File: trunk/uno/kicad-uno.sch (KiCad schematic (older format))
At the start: 17 parts, among them J1 RESET_EN, SW1 RESET

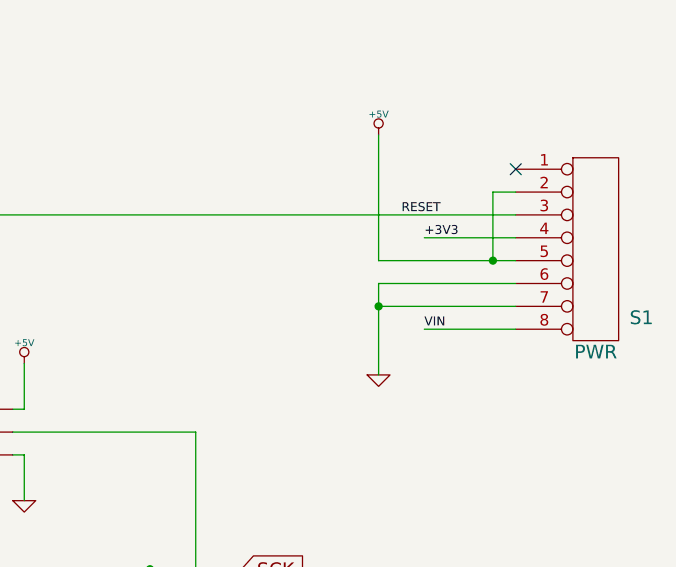
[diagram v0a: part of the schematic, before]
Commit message: Schematic ERC passes. Circuit _might_ be complete, without errors. You just never know. :-P
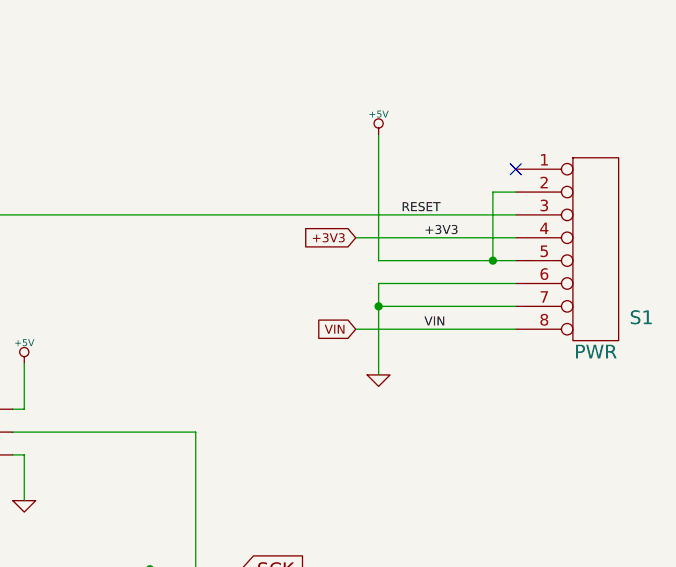
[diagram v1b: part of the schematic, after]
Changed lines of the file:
@@
 Connection ~ 3750 2150
-Wire Wire Line
-	8350 1450 7950 1450
 Wire Wire Line
 	8350 1650 7750 1650
@@
 	8350 1750 7750 1750
 Connection ~ 7750 1750
-Wire Wire Line
-	8350 1850 7950 1850
 Connection ~ 6950 3900
 Connection ~ 6850 3800
@@
 	7950 3600 7950 4350
 Connection ~ 6750 2900
+Text GLabel 7650 1450 0    39   Input ~ 0
++3V3
+Wire Wire Line
+	8350 1450 7650 1450
+Text GLabel 7650 1850 0    39   Input ~ 0
+VIN
+Wire Wire Line
+	8350 1850 7650 1850
 $EndSCHEMATC

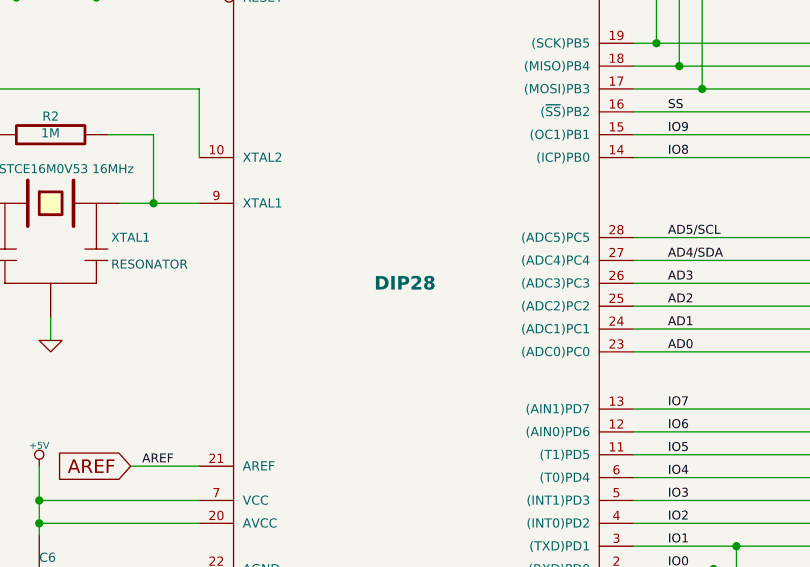
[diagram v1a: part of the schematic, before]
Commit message: Component packages configured.
PCB initial placement.

Some minor typo corrections.
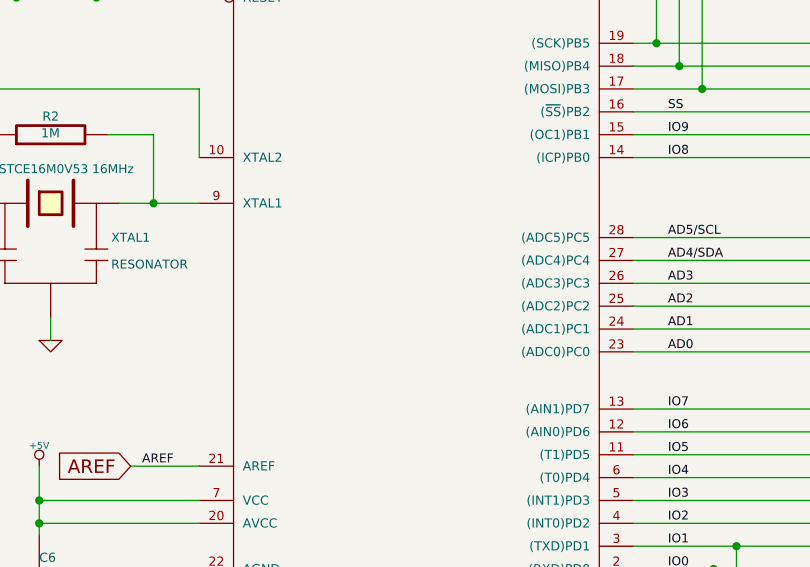
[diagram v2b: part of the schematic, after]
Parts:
- C5, C6: footprint ~ -> SM0603_Capa
- D2: footprint ~ -> SM1206D
- ICSP1: footprint (none) -> pin_array_3x2
- J1: footprint ~ -> JSOLD
- R2, RN1D1, RN2D1, RN4A1, RN4B1, SW1, XTAL1: footprint ~ -> (none)
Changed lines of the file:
@@
 Sheet 1 3
 Title "KiCADuino UNO Rev3"
-Date "24 jul 2013"
+Date "25 jul 2013"
 Rev "0.1"
 Comp "Gruvin & Co"
@@
 F 0 "R2" V 4180 4100 40  0000 C CNN
 F 1 "1M" V 4107 4101 40  0000 C CNN
-F 2 "~" V 4030 4100 30  0000 C CNN
+F 2 "" V 4030 4100 30  0001 C CNN
 F 3 "~" H 4100 4100 30  0000 C CNN
 	1    4100 4100
@@
 F 0 "XTAL1" H 4450 4250 39  0000 C CNN
 F 1 "CSTCE16M0V53 16MHz" H 4150 4550 39  0000 C CNN
-F 2 "~" H 4100 4400 60  0000 C CNN
+F 2 "" H 4100 4400 60  0001 C CNN
 F 3 "~" H 4100 4400 60  0000 C CNN
 	1    4100 4400
@@
 F 0 "ZU4" H 4950 6300 47  0000 L BNN
 F 1 "ATMEGA328P-PU" H 5850 3200 47  0000 L BNN
-F 2 "DIP28" H 5650 4850 59  0000 C CNB
+F 2 "DIP28" H 5650 4850 59  0001 C CNB
 F 3 "~" H 5650 4800 60  0000 C CNN
 	1    5650 4800
@@
 F 0 "C6" H 4050 6150 40  0000 L CNN
 F 1 "100n" H 4056 5965 40  0000 L CNN
-F 2 "~" H 4088 5900 30  0000 C CNN
+F 2 "SM0603_Capa" H 4088 5900 30  0001 C CNN
 F 3 "~" H 4050 6050 60  0000 C CNN
 	1    4050 6050
@@
 F 0 "D2" H 4300 3300 40  0000 C CNN
 F 1 "CD1206-S01575" H 4300 3100 40  0000 C CNN
-F 2 "~" H 4300 3200 60  0000 C CNN
+F 2 "SM1206D" H 4300 3200 60  0001 C CNN
 F 3 "~" H 4300 3200 60  0000 C CNN
 	1    4300 3200
@@
 F 0 "RN1D1" V 4030 3200 40  0000 C CNN
 F 1 "10K" V 3957 3201 40  0000 C CNN
-F 2 "~" V 3880 3200 30  0000 C CNN
+F 2 "" V 3880 3200 30  0001 C CNN
 F 3 "~" H 3950 3200 30  0000 C CNN
 	1    3950 3200
@@
 F 0 "ICSP1" H 5750 2600 50  0000 C CNN
 F 1 "3X2 M" H 5750 2200 40  0000 C CNN
-F 2 "" H 5750 2350 60  0000 C CNN
+F 2 "pin_array_3x2" H 5750 2350 60  0001 C CNN
 F 3 "" H 5750 2350 60  0000 C CNN
 	1    5750 2350
@@
 F 0 "SW1" V 4200 2300 60  0000 L CNN
 F 1 "RESET" V 4350 2300 60  0000 L CNN
-F 2 "~" H 4300 1950 60  0000 C CNN
+F 2 "" H 4300 1950 60  0001 C CNN
 F 3 "~" H 4300 1950 60  0000 C CNN
 	1    4300 1950
@@
 F 0 "J1" H 3350 2300 60  0000 C CNN
 F 1 "RESET_EN" H 3350 2070 40  0000 C CNN
-F 2 "~" H 3350 2150 60  0000 C CNN
+F 2 "JSOLD" H 3350 2150 60  0001 C CNN
 F 3 "~" H 3350 2150 60  0000 C CNN
 	1    3350 2150
@@
 F 0 "C5" V 2750 2250 40  0000 L CNN
 F 1 "100n" V 2650 2200 40  0000 L CNN
-F 2 "~" H 2738 2250 30  0000 C CNN
+F 2 "SM0603_Capa" H 2738 2250 30  0001 C CNN
 F 3 "~" H 2700 2400 60  0000 C CNN
 	1    2700 2400
@@
 F 0 "S4" H 8900 4150 60  0000 C CNN
 F 1 "IOH" H 8700 4300 60  0000 C CNN
-F 2 "" H 8700 3750 60  0000 C CNN
+F 2 "" H 8700 3750 60  0001 C CNN
 F 3 "" H 8700 3750 60  0000 C CNN
 	1    8700 3750
@@
 F 0 "S2" H 8900 5000 60  0000 C CNN
 F 1 "AD" H 8700 5150 60  0000 C CNN
-F 2 "" H 8700 4800 60  0000 C CNN
+F 2 "" H 8700 4800 60  0001 C CNN
 F 3 "" H 8700 4800 60  0000 C CNN
 	1    8700 4800
@@
 F 0 "S3" H 8900 5950 60  0000 C CNN
 F 1 "IOL" H 8700 6150 60  0000 C CNN
-F 2 "" H 8700 5650 60  0000 C CNN
+F 2 "" H 8700 5650 60  0001 C CNN
 F 3 "" H 8700 5650 60  0000 C CNN
 	1    8700 5650
@@
 F 0 "S1" H 8900 1200 60  0000 C CNN
 F 1 "PWR" H 8700 1050 60  0000 C CNN
-F 2 "" H 8700 1500 60  0000 C CNN
+F 2 "" H 8700 1500 60  0001 C CNN
 F 3 "" H 8700 1500 60  0000 C CNN
 	1    8700 1500
@@
 F 0 "RN4B1" V 7680 6200 40  0000 C CNN
 F 1 "1K" V 7607 6201 40  0000 C CNN
-F 2 "~" V 7530 6200 30  0000 C CNN
+F 2 "" V 7530 6200 30  0001 C CNN
 F 3 "~" H 7600 6200 30  0000 C CNN
 	1    7600 6200
@@
 F 0 "RN4A1" V 7680 6400 40  0000 C CNN
 F 1 "1K" V 7607 6401 40  0000 C CNN
-F 2 "~" V 7530 6400 30  0000 C CNN
+F 2 "" V 7530 6400 30  0001 C CNN
 F 3 "~" H 7600 6400 30  0000 C CNN
 	1    7600 6400
@@
 F 0 "RN2D1" V 2380 2850 40  0000 C CNN
 F 1 "1K" V 2307 2851 40  0000 C CNN
-F 2 "~" V 2230 2850 30  0000 C CNN
+F 2 "" V 2230 2850 30  0001 C CNN
 F 3 "~" H 2300 2850 30  0000 C CNN
 	1    2300 2850

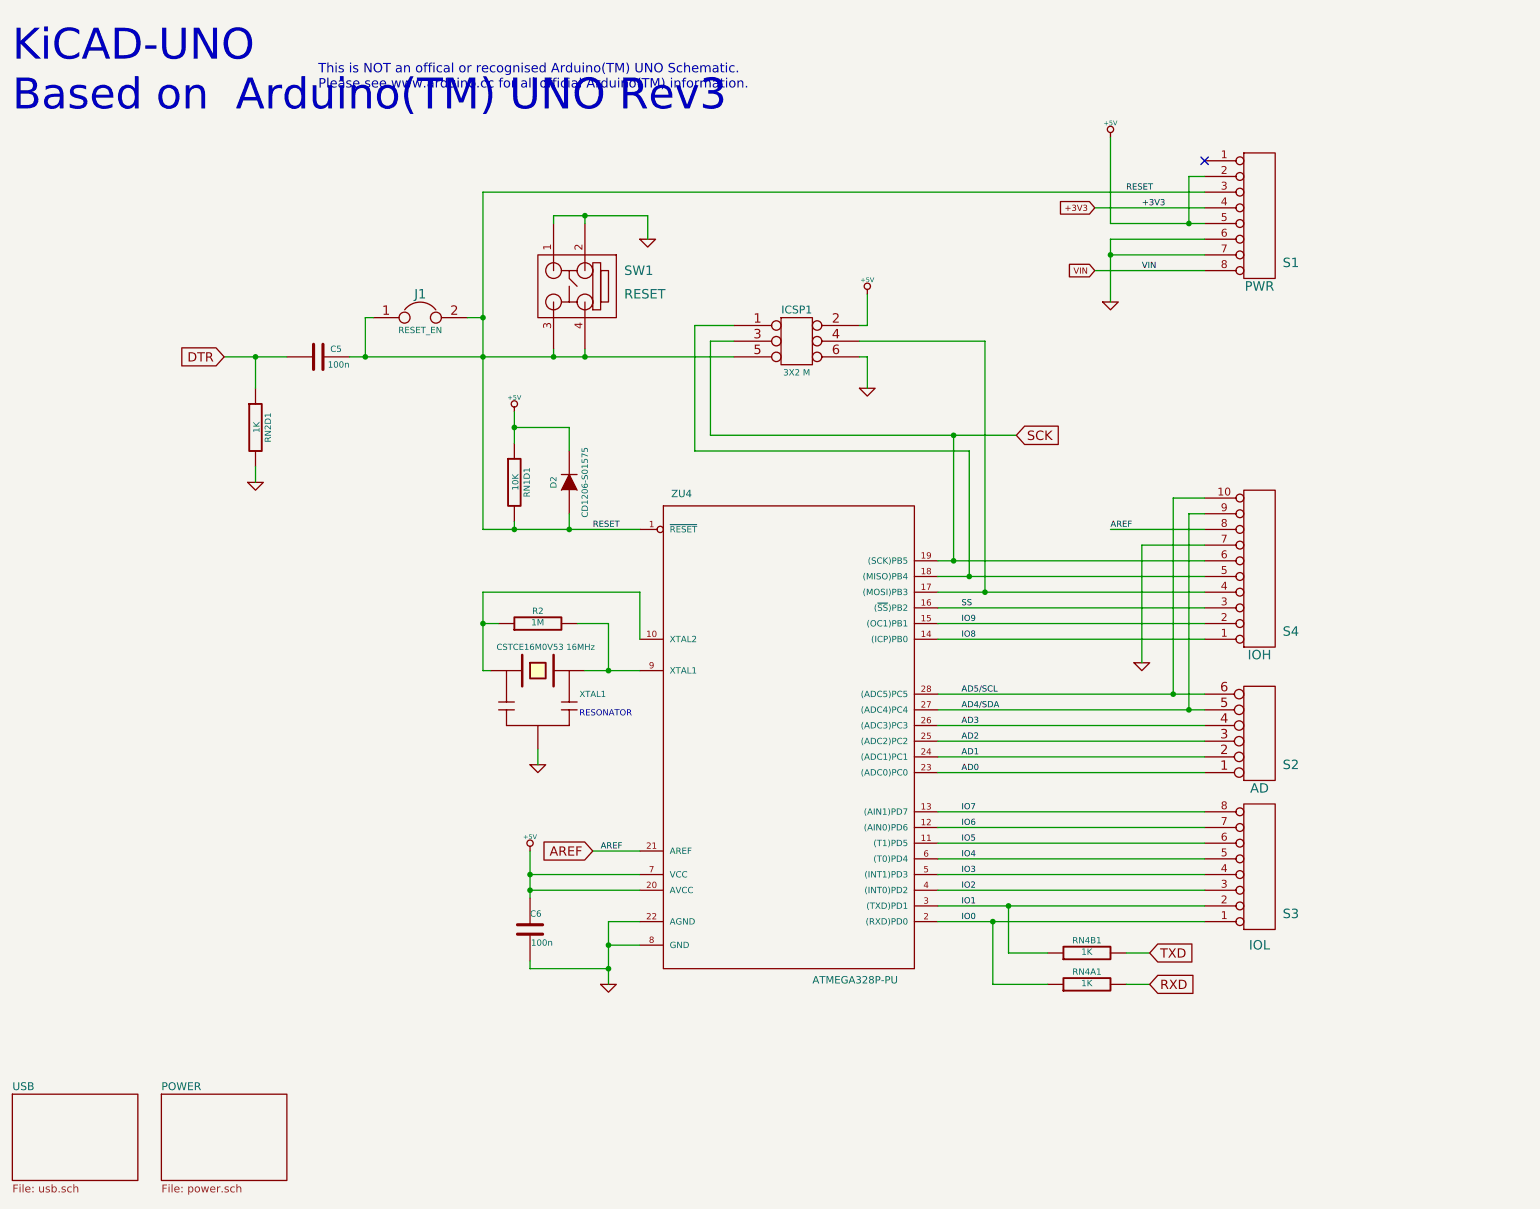
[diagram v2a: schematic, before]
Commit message: Added resistor network part/module for RN1-4 (no 3D package yet).
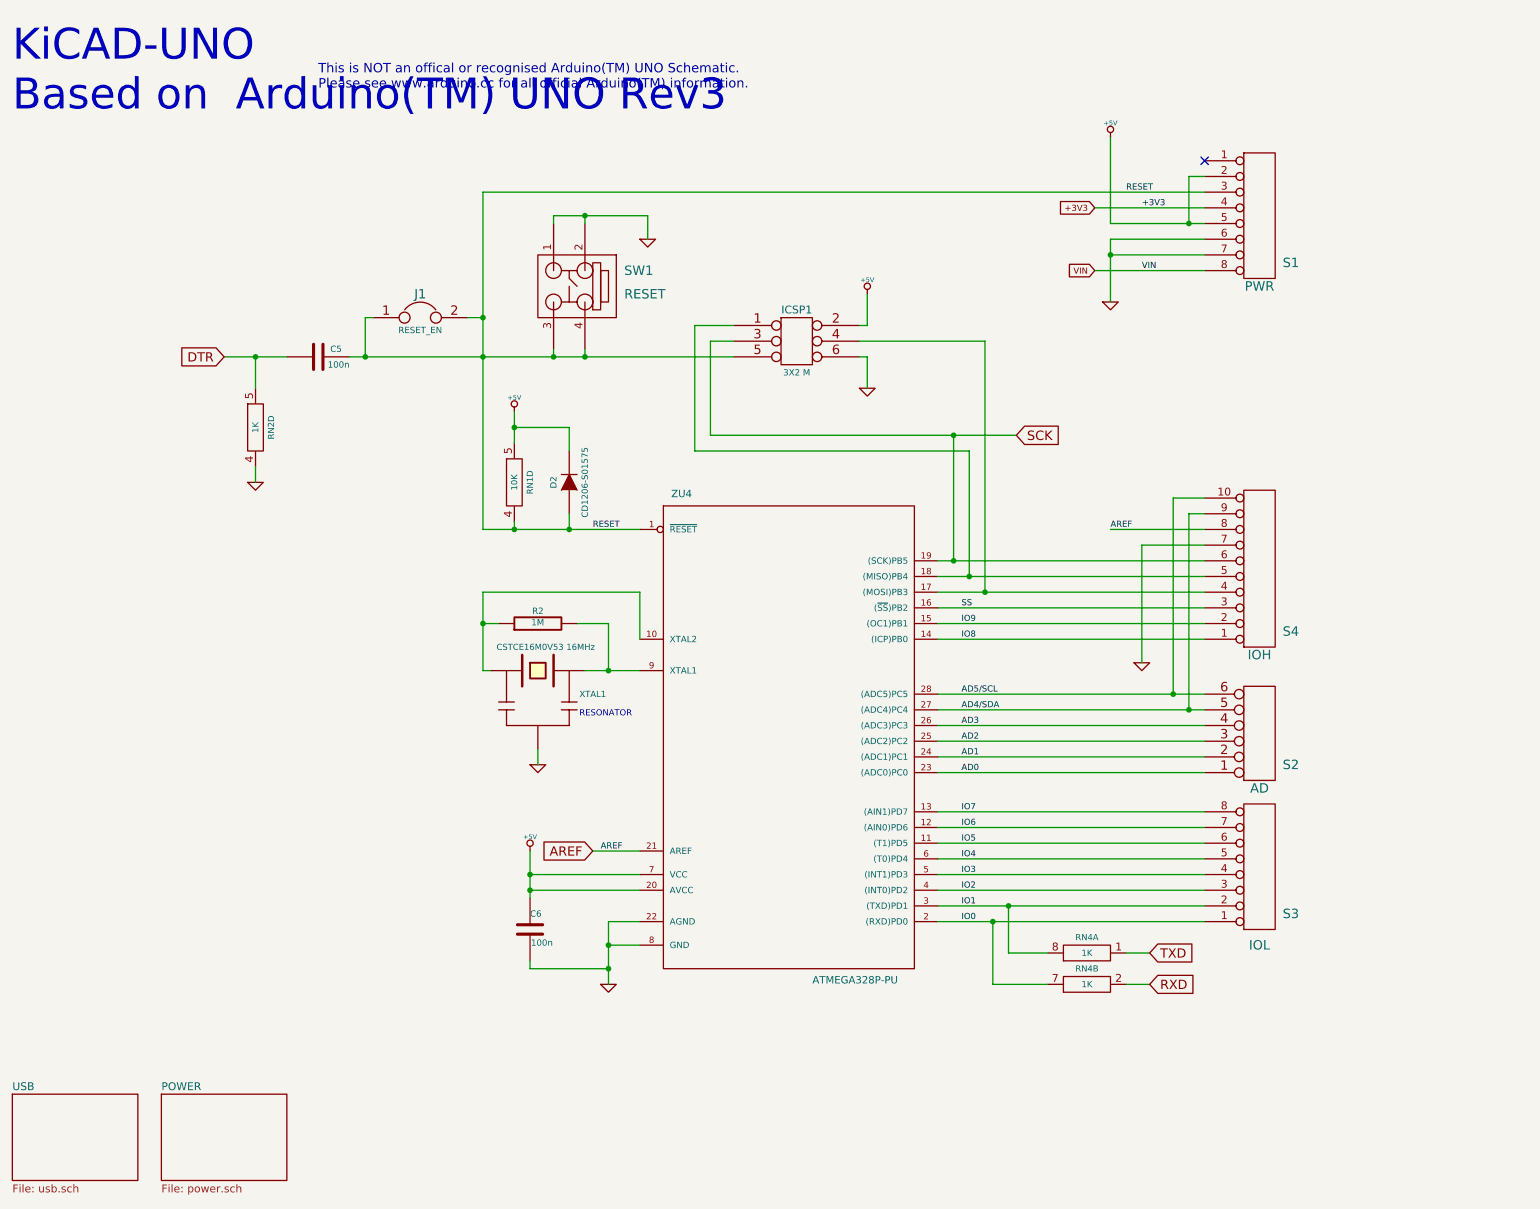
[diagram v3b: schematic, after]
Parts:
- removed RN1D1: 10K, symbol R
- removed RN2D1, RN4A1, RN4B1: 1K, symbol R
- added RN1: 10K, symbol R_NET4
- added RN2, RN4: 1K, symbol R_NET4
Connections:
- net +5V: now also RN1.5 (6)
- net DTR: now also RN2.5 (6)
- net GND: now also RN2.4 (3)
- net IO0: now also RN4.7 (6)
- net IO1: now also RN4.8 (6)
- net RESET: now also RN1.4 (3)
- net RXD: now also RN4.2 (3)
- net TXD: now also RN4.1 (3)
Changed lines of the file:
@@
 	0    -1   -1   0
-$EndComp
-$Comp
-L R RN1D1
-U 1 1 51EFB493
-P 3950 3200
-F 0 "RN1D1" V 4030 3200 40  0000 C CNN
-F 1 "10K" V 3957 3201 40  0000 C CNN
-F 2 "" V 3880 3200 30  0001 C CNN
-F 3 "~" H 3950 3200 30  0000 C CNN
-	1    3950 3200
-	1    0    0    -1
 $EndComp
 Text Label 4450 3500 0    39   ~ 0
@@
 Text GLabel 8000 6200 2    59   Input ~ 0
 TXD
-$Comp
-L R RN4B1
-U 1 1 51EFD800
-P 7600 6200
-F 0 "RN4B1" V 7680 6200 40  0000 C CNN
-F 1 "1K" V 7607 6201 40  0000 C CNN
-F 2 "" V 7530 6200 30  0001 C CNN
-F 3 "~" H 7600 6200 30  0000 C CNN
-	1    7600 6200
-	0    -1   -1   0
-$EndComp
-$Comp
-L R RN4A1
-U 1 1 51EFD806
-P 7600 6400
-F 0 "RN4A1" V 7680 6400 40  0000 C CNN
-F 1 "1K" V 7607 6401 40  0000 C CNN
-F 2 "" V 7530 6400 30  0001 C CNN
-F 3 "~" H 7600 6400 30  0000 C CNN
-	1    7600 6400
-	0    -1   -1   0
-$EndComp
 $Sheet
 S 750  7100 800  550
@@
 F1 "usb.sch" 50
 $EndSheet
-$Comp
-L R RN2D1
-U 1 1 51EFF96D
-P 2300 2850
-F 0 "RN2D1" V 2380 2850 40  0000 C CNN
-F 1 "1K" V 2307 2851 40  0000 C CNN
-F 2 "" V 2230 2850 30  0001 C CNN
-F 3 "~" H 2300 2850 30  0000 C CNN
-	1    2300 2850
-	1    0    0    -1
-$EndComp
 $Comp
 L GND #PWR011
@@
 Wire Wire Line
 	8350 1850 7650 1850
+$Comp
+L R_NET4 RN1
+U 4 1 51F10FC8
+P 3950 3200
+F 0 "RN1" V 4050 3200 39  0000 C CNN
+F 1 "10K" V 3950 3200 39  0000 C CNN
+F 2 "" H 3950 3200 60  0000 C CNN
+F 3 "" H 3950 3200 60  0000 C CNN
+	4    3950 3200
+	1    0    0    -1
+$EndComp
+$Comp
+L R_NET4 RN2
+U 4 1 51F11ACB
+P 2300 2850
+F 0 "RN2" V 2400 2850 39  0000 C CNN
+F 1 "1K" V 2300 2850 39  0000 C CNN
+F 2 "" H 2300 2850 60  0000 C CNN
+F 3 "" H 2300 2850 60  0000 C CNN
+	4    2300 2850
+	1    0    0    -1
+$EndComp
+$Comp
+L R_NET4 RN4
+U 1 1 51F121CA
+P 7600 6200
+F 0 "RN4" V 7700 6200 39  0000 C CNN
+F 1 "1K" V 7600 6200 39  0000 C CNN
+F 2 "" H 7600 6200 60  0000 C CNN
+F 3 "" H 7600 6200 60  0000 C CNN
+	1    7600 6200
+	0    -1   -1   0
+$EndComp
+$Comp
+L R_NET4 RN4
+U 2 1 51F121D7
+P 7600 6400
+F 0 "RN4" V 7700 6400 39  0000 C CNN
+F 1 "1K" V 7600 6400 39  0000 C CNN
+F 2 "" H 7600 6400 60  0000 C CNN
+F 3 "" H 7600 6400 60  0000 C CNN
+	2    7600 6400
+	0    -1   -1   0
+$EndComp
 $EndSCHEMATC
